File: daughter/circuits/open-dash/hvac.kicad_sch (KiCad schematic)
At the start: 31 parts, among them Q3 Q_NPN_BEC, Q4 Q_NPN_BEC, Q5 Q_NPN_BEC, Q6 Q_NPN_BEC, Q7 Q_NPN_BEC, Q8 Q_NPN_BEC, U13 MCP23017_SS, U14 ADC_ADS1015, U15 ADC_ADS1015, U16 ADC_ADS1015

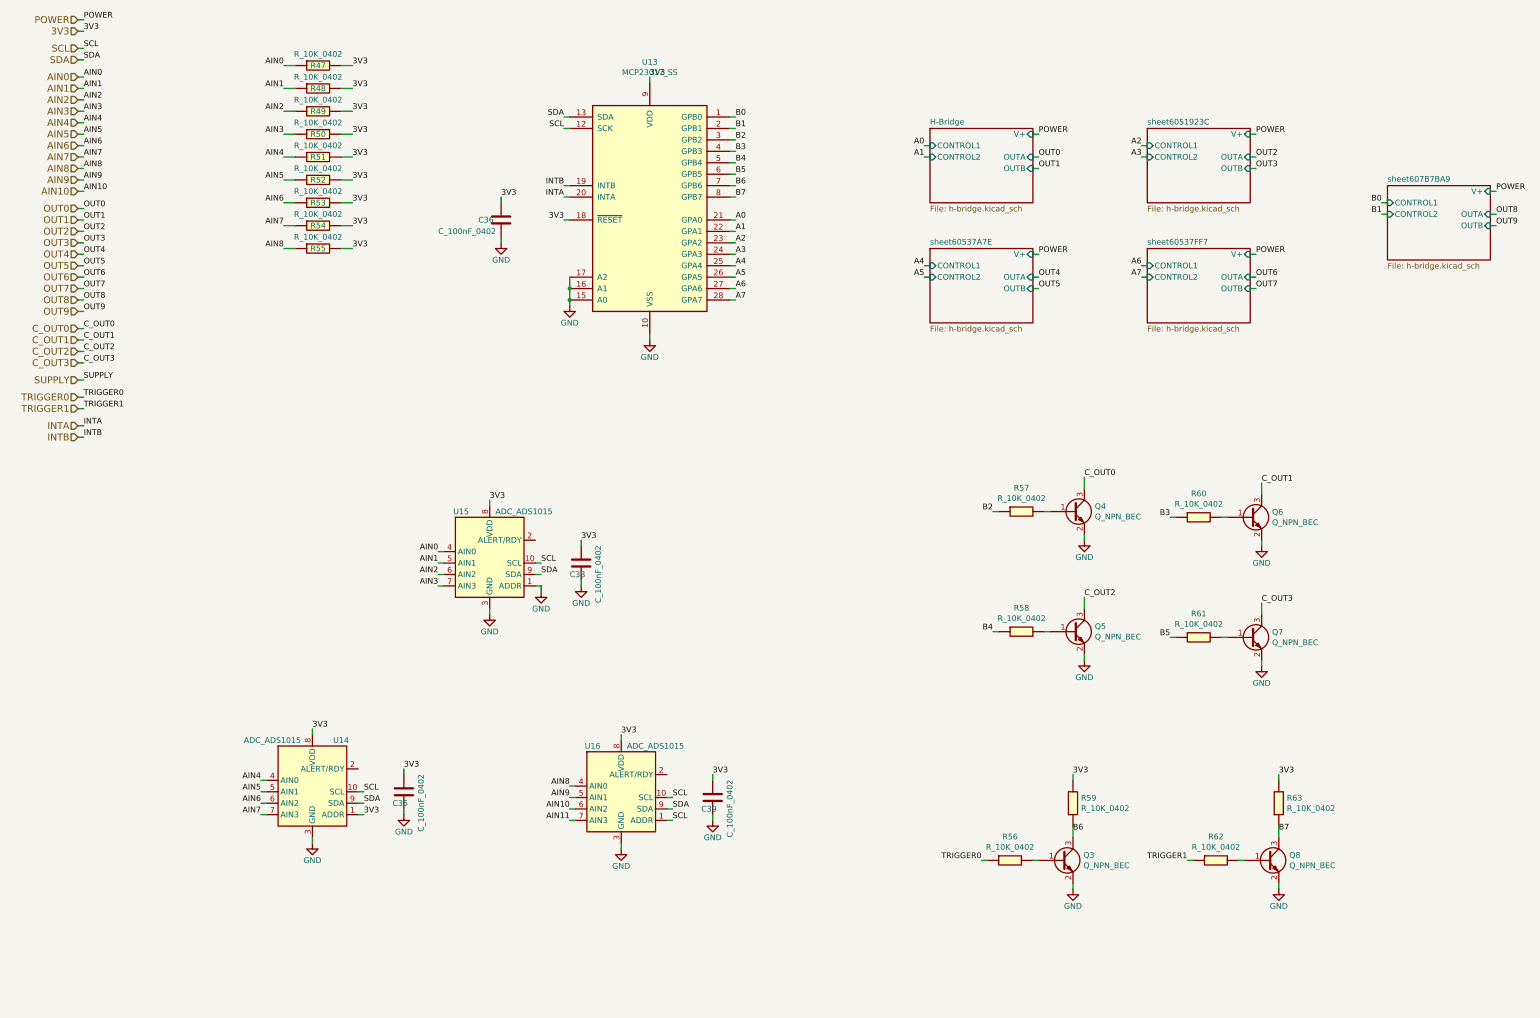
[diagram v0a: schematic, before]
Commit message: Updated hvac circuit
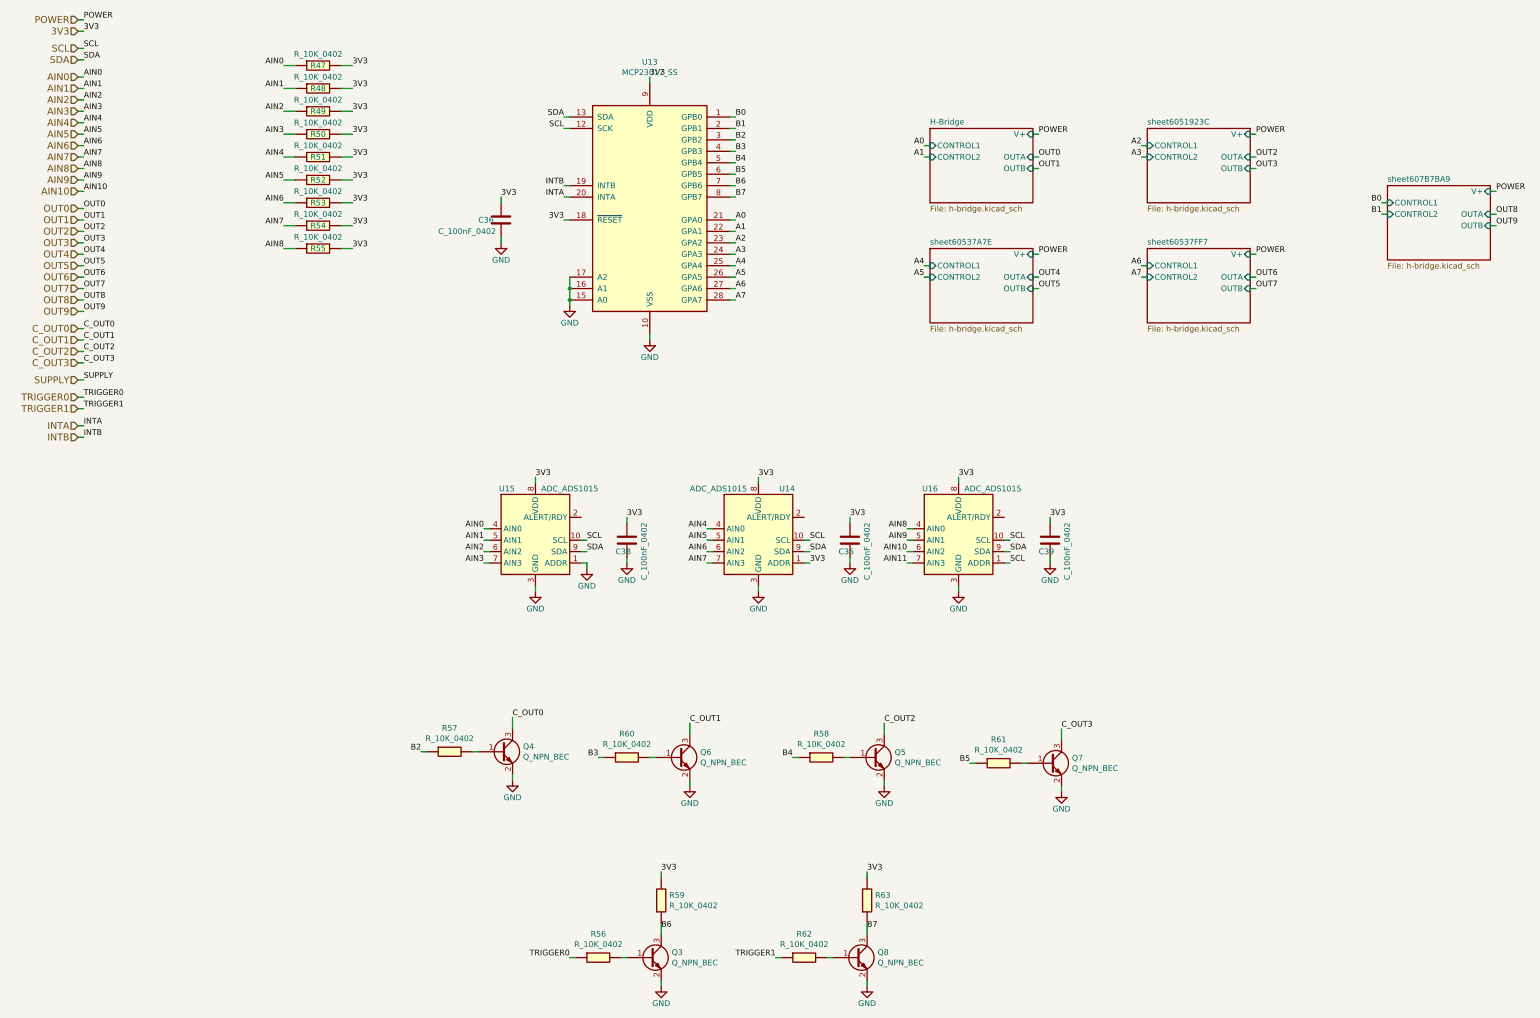
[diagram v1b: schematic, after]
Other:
- moved on the sheet: C35, C38, C39, Q3, Q4, Q5, Q6, Q7, Q8, R56, R57, R58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
